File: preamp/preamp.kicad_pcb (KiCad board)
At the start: 2 copper layers, 19 parts, among them J1 XLR3_AudioJack2_Combo, J2 Output, J4 AudioJack3_Switch, U1 SSM2019

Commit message: Prepare for routing
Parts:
- C7: footprint Capacitor_THT:C_Disc_D3.0mm_W1.6mm_P2.50mm -> Capacitor_THT:C_Rect_L7.0mm_W2.5mm_P5.00mm
- J1: footprint Connector_Audio:Jack_XLR-6.35mm_Neutrik_NCJ9FI-V-0_Vertical -> Connector_Audio:Jack_XLR_Neutrik_NC3FAAH2_Horizontal
- moved R4 53.0 mm to (81.4, 43.4)
- moved BT1 52.8 mm to (148.8, 46.6)
- moved BT2 52.8 mm to (137.8, 46.6)
- moved C7 38.1 mm to (137.9, 79.2), turned to 90 degrees
- moved C4 37.9 mm to (97.1, 77.8), turned to 0 degrees
- moved R1 35.8 mm to (101.0, 73.6), turned to 0 degrees
- moved R3 35.6 mm to (101.1, 76.5), turned to 0 degrees
- moved C1 33.6 mm to (104.5, 68.4), turned to -90 degrees
- moved J1 33.4 mm to (111.2, 84.8), turned to -90 degrees
- moved C2 27.5 mm to (98.1, 81.9), turned to -90 degrees
- moved U1 19.1 mm to (128.4, 75.3), turned to 0 degrees
- moved C6 17.5 mm to (125.9, 79.8), turned to 90 degrees
- moved J2 17.3 mm to (147.0, 85.9), turned to 90 degrees
- moved C5 15.4 mm to (123.0, 63.1), turned to 0 degrees
- moved R5 15.2 mm to (135.9, 85.8), turned to 180 degrees
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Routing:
- net Net-(J2-Pad2): track 0.00 -> 23.7 mm
- net Net-(RV1-Pad3): track 0.00 -> 21.3 mm
- net Net-(C2-Pad1): track 0.00 -> 16.8 mm
- net Net-(R5-Pad2): track 0.00 -> 12.0 mm
- net Net-(R5-Pad1): track 0.00 -> 9.85 mm
- net Net-(C4-Pad2): track 0.00 -> 2.80 mm
- net Net-(C5-Pad2): track 0.00 -> 2.79 mm
- net Net-(U1-Pad6): track 0.00 -> 2.33 mm

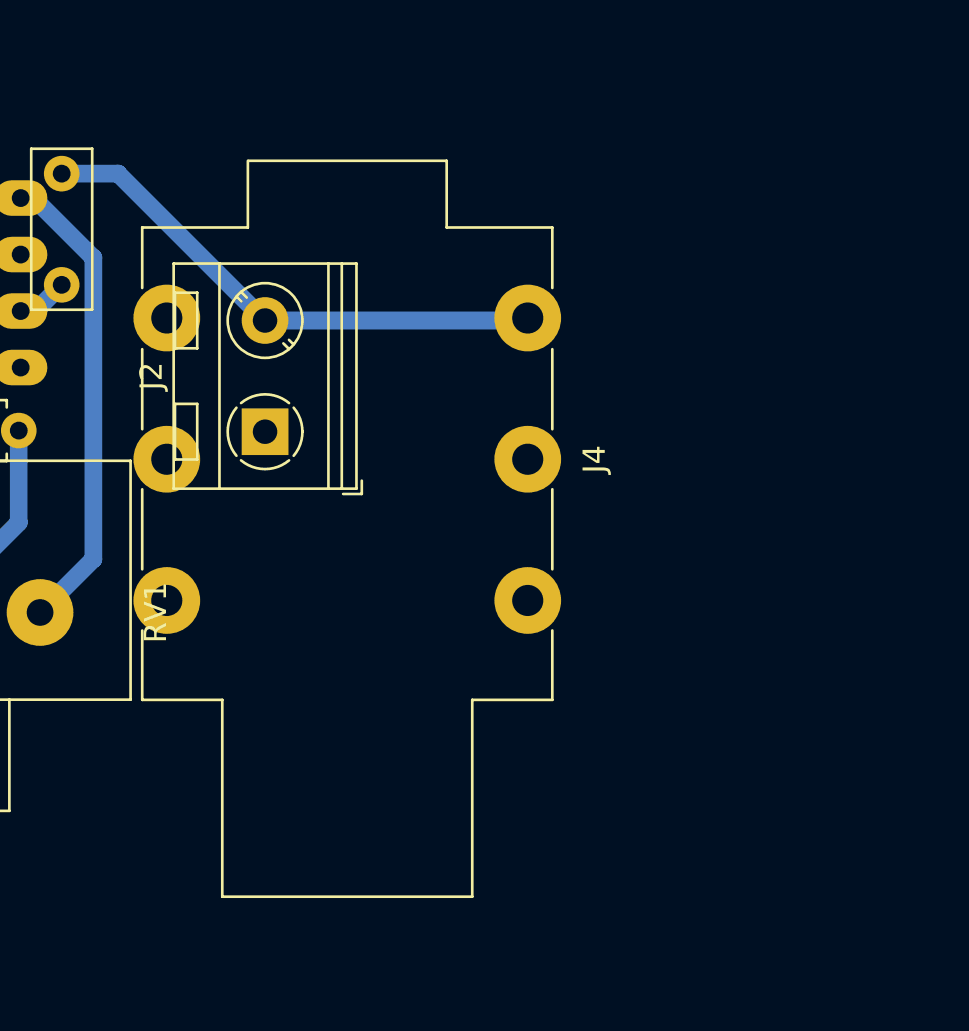
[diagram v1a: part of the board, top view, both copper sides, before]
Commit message: Add RCA Plug
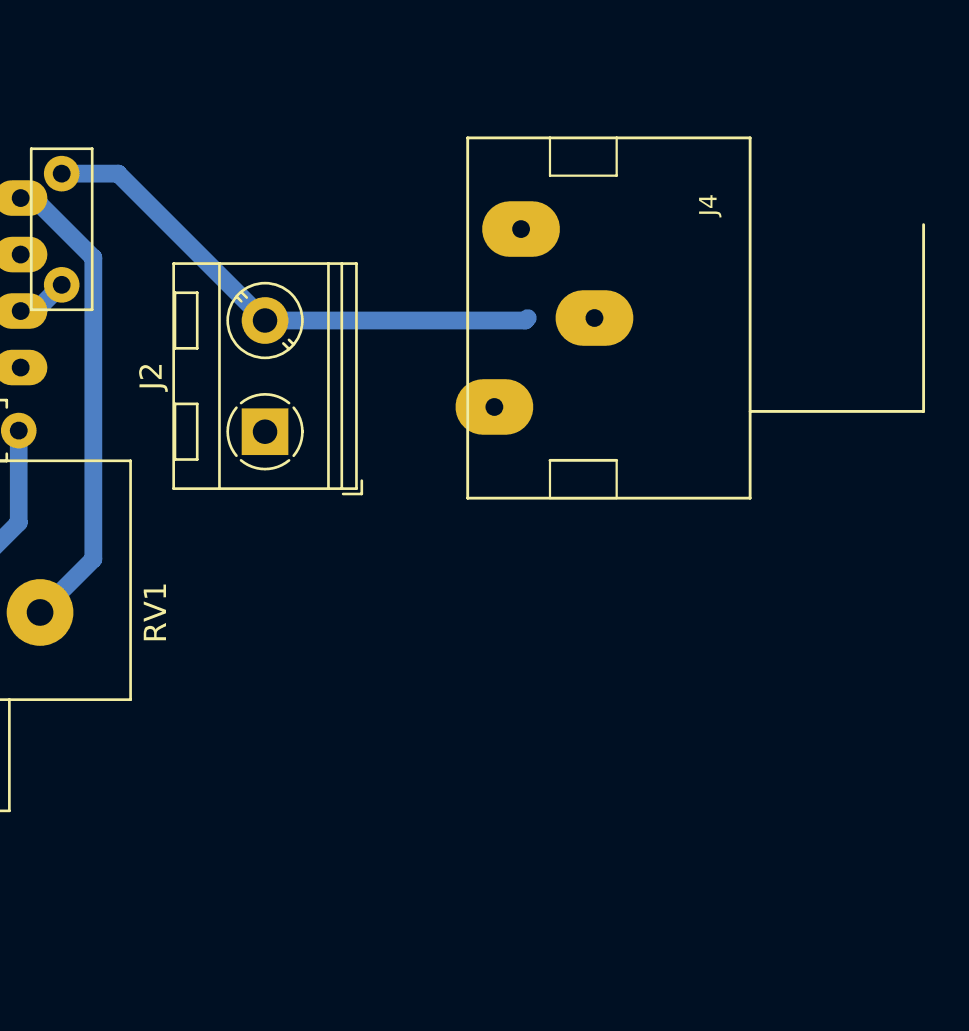
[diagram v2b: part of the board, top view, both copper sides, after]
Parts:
- J4: value AudioJack3_Switch -> RCJ-22; footprint Connector_Audio:Jack_6.35mm_Neutrik_NMJ6HFD2-AU_Horizontal -> rcj-22:rcj-22
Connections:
- C7 pad 2: Net-(J2-Pad2) -> Net-(C7-Pad2)
- J2 pad 2: Net-(J2-Pad2) -> Net-(C7-Pad2)
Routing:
- net Net-(J2-Pad2): track 23.7 -> 0.00 mm
- net Net-(C7-Pad2): track 0.00 -> 23.7 mm

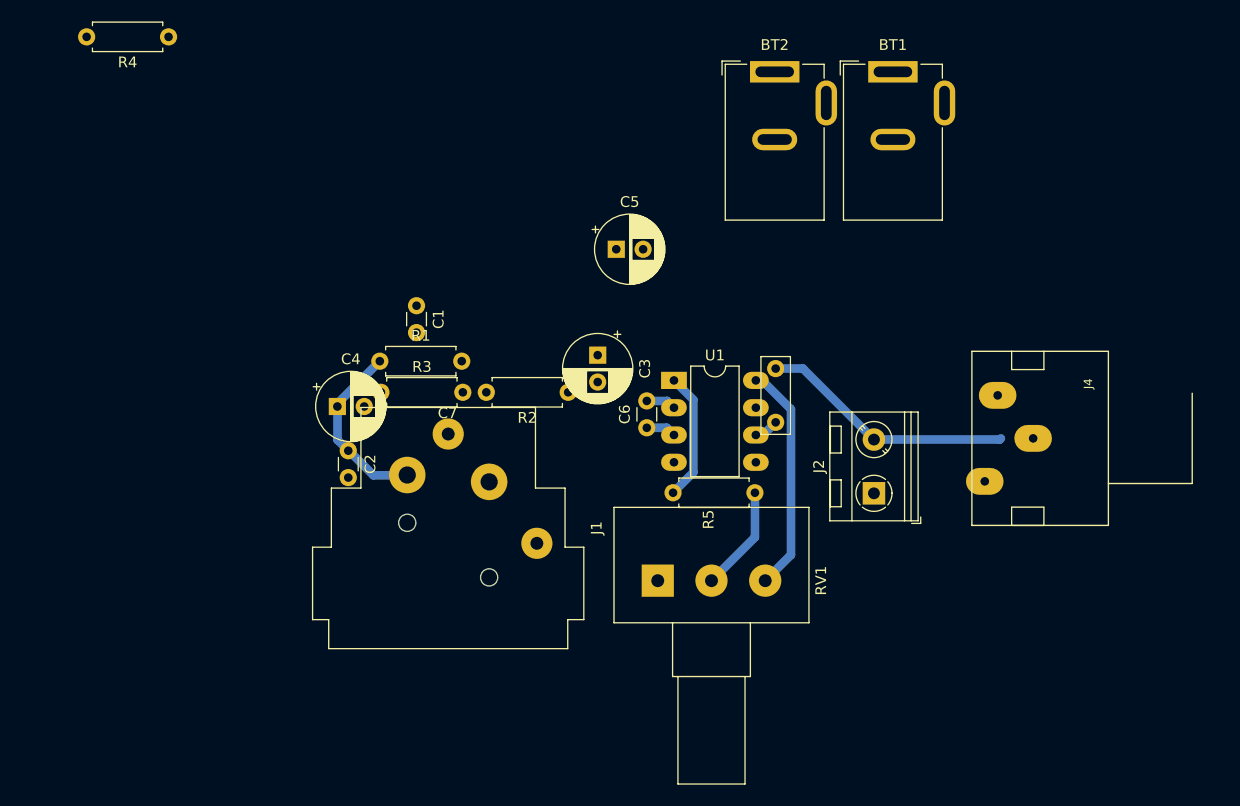
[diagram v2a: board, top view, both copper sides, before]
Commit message: Routing of preamp
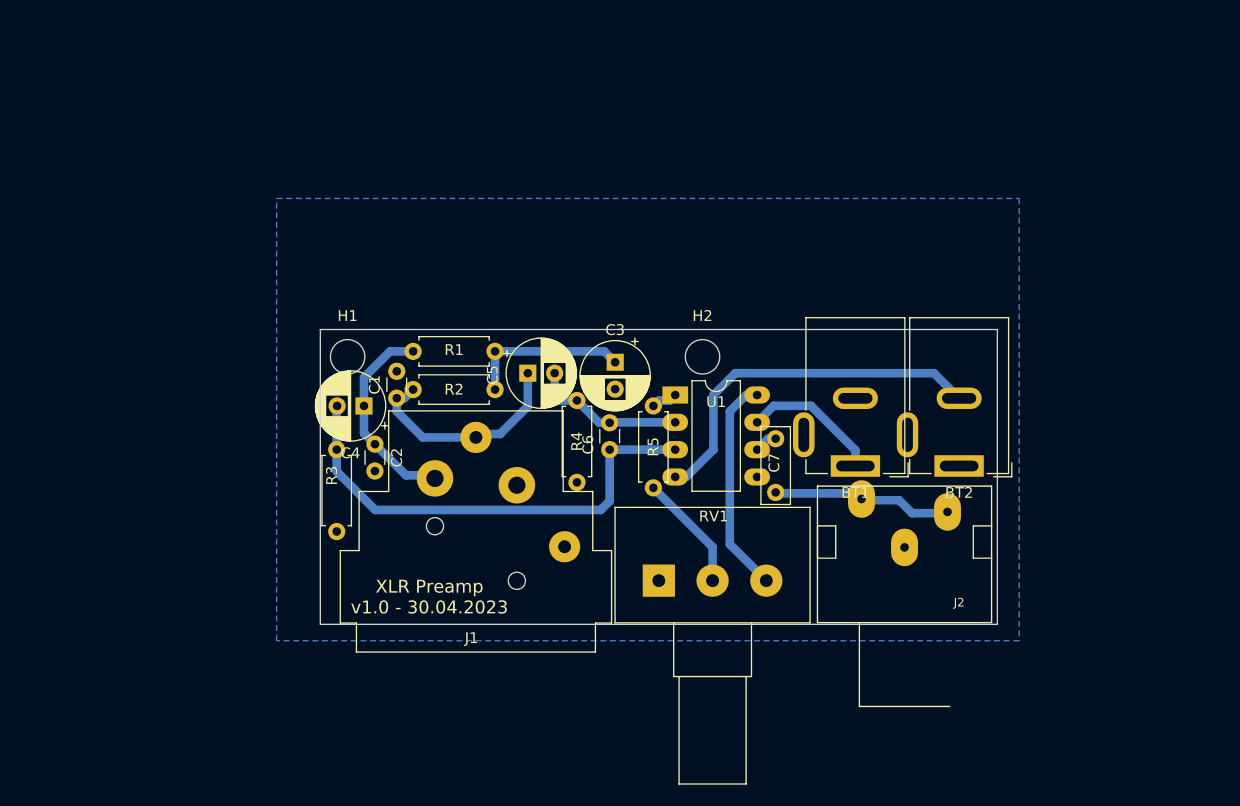
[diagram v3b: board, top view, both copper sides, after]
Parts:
- removed J4: RCJ-22, rcj-22:rcj-22
- added H1: MountingHole, MountingHole:MountingHole_3.2mm_M3_DIN965, F.Cu at (98.0, 73.2)
- added H2: MountingHole, MountingHole:MountingHole_3.2mm_M3_DIN965, F.Cu at (131.1, 73.2)
- J2: value Output -> RCJ-22; footprint TerminalBlock_RND:TerminalBlock_RND_205-00045_1x02_P5.00mm_Horizontal -> rcj-22:rcj-22
- moved R4 56.2 mm to (119.4, 84.8), turned to 90 degrees
- moved BT2 40.5 mm to (154.9, 83.3), turned to 180 degrees
- moved BT1 36.8 mm to (145.3, 83.3), turned to 180 degrees
- moved C5 14.2 mm to (114.8, 74.7)
- moved R5 9.46 mm to (126.5, 85.3), turned to 90 degrees
- moved C1 8.80 mm to (102.6, 77.0), turned to 90 degrees
- moved R2 6.81 mm to (111.8, 76.2)
- moved R3 6.74 mm to (97.0, 81.8), turned to -90 degrees
- moved C6 4.01 mm to (122.4, 81.8)
- moved J2 3.50 mm to (149.9, 87.9), turned to 180 degrees
- moved R1 3.23 mm to (104.1, 72.6)
- moved J1 2.60 mm to (113.8, 85.1)
- moved C2 2.55 mm to (100.6, 81.3)
- moved C4 2.48 mm to (99.6, 77.7), turned to 180 degrees
- moved C3 1.75 mm to (122.9, 73.7)
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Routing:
- net Net-(C4-Pad2): track 2.80 -> 44.2 mm
- net -15V: track 0.00 -> 34.4 mm
- net Net-(C1-Pad1): track 0.00 -> 20.6 mm
- net Net-(C3-Pad1): track 0.00 -> 15.2 mm
- net +15V: track 0.00 -> 13.0 mm
- net Net-(C5-Pad2): track 2.79 -> 14.3 mm
- net Net-(R5-Pad2): track 12.0 -> 2.45 mm
- net Net-(C7-Pad2): track 23.7 -> 16.8 mm
- net Net-(C2-Pad1): track 16.8 -> 19.1 mm
- net Net-(R5-Pad1): track 9.85 -> 10.9 mm
- net Net-(RV1-Pad3): track 21.3 -> 20.3 mm
- added copper zone on B.Cu, net GNDA
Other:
- board outline added: 63 x 27.4 mm
- board text added: "XLR Preamp v1.0 - 30.04.2023"

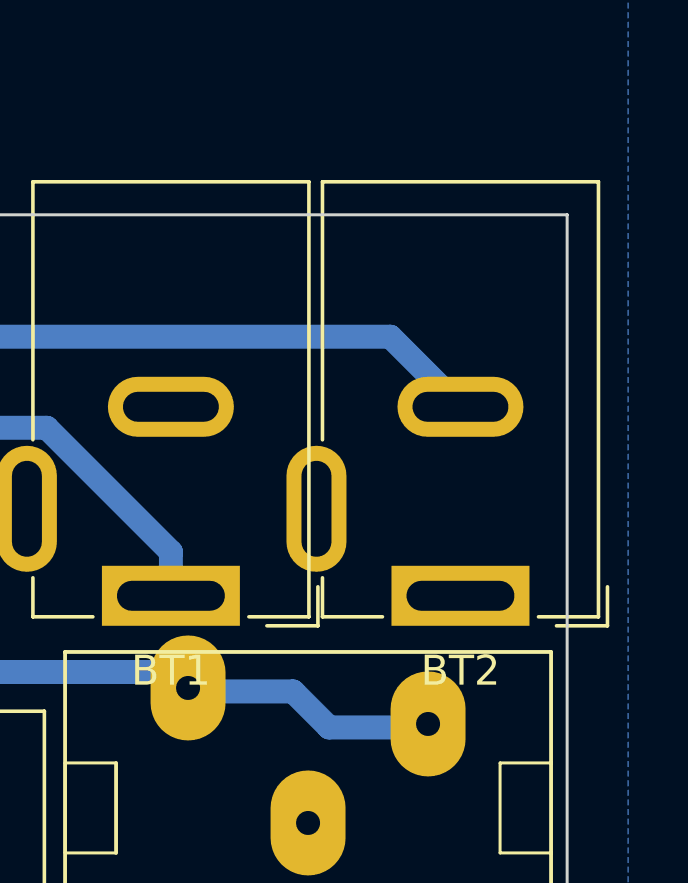
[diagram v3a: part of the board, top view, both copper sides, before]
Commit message: Add 3d models
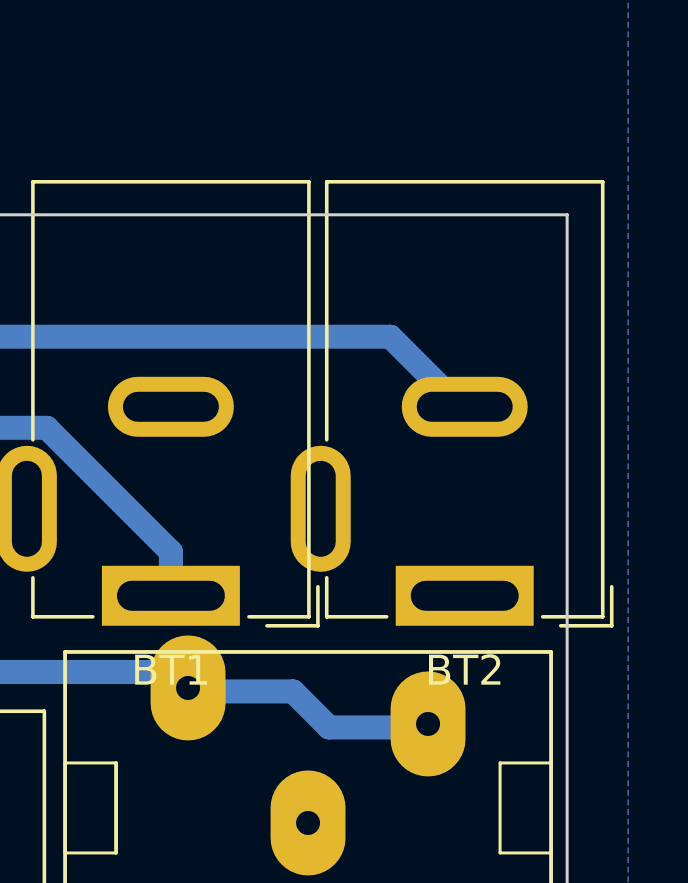
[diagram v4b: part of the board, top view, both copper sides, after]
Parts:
- moved BT2 0.14 mm to (155.1, 83.3)
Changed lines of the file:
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@@
       (rotate (xyz 0 0 0))
+    )
+    (model "${KIPRJMOD}/lib/potentiometer.step"
+      (offset (xyz 5.75 -5 12.5))
+      (scale (xyz 1 1 1))
+      (rotate (xyz 90 -180 -90))
     )
   )
@@
       (scale (xyz 1 1 1))
       (rotate (xyz 0 0 0))
+    )
+  )
+  (footprint "Connector_BarrelJack:BarrelJack_GCT_DCJ200-10-A_Horizontal" (layer "F.Cu")
+    (at 155.082 83.312 180)
+    (descr "Barrel jack connector (5.5 mm outer diameter, 2.05 inner diameter ), https://gct.co/files/drawings/dcj200-10.pdf")
+    (tags "connector barrel jack")
+    (property "Sheetfile" "preamp.kicad_sch")
+    (property "Sheetname" "")
+    (attr through_hole)
+    (fp_text reference "BT2" (at 0 -2.5) (layer "F.SilkS")
+      (effects (font (size 1 1) (thickness 0.15)))
+    )
+    (fp_text value "Battery_Cell" (at 0 15.5) (layer "F.Fab")
+      (effects (font (size 1 1) (thickness 0.15)))
+    )
+    (fp_text user "${REFERENCE}" (at 0 3) (layer "F.Fab")
+      (effects (font (size 1 1) (thickness 0.15)))
+    )
+    (fp_line (start -4.6 13.8) (end -4.6 -0.7) (layer "F.SilkS") (width 0.12))
+    (fp_line (start -4.6 -0.7) (end -2.6 -0.7) (layer "F.SilkS") (width 0.12))
+    (fp_line (start 4.6 13.8) (end -4.6 13.8) (layer "F.SilkS") (width 0.12))
+    (fp_line (start 2.6 -0.7) (end 4.6 -0.7) (layer "F.SilkS") (width 0.12))
+    (fp_line (start 4.6 5.2) (end 4.6 13.8) (layer "F.SilkS") (width 0.12))
+    (fp_line (start 4.6 -0.7) (end 4.6 0.6) (layer "F.SilkS") (width 0.12))
+    (fp_line (start -4.9 -1) (end -4.9 0.3) (layer "F.SilkS") (width 0.12))
+    (fp_line (start -3.2 -1) (end -4.9 -1) (layer "F.SilkS") (width 0.12))
+    (fp_line (start 6.3 5.5) (end 5 5.5) (layer "F.CrtYd") (width 0.05))
+    (fp_line (start 5 -1.5) (end -5 -1.5) (layer "F.CrtYd") (width 0.05))
+    (fp_line (start 5 14.2) (end 5 5.5) (layer "F.CrtYd") (width 0.05))
+    (fp_line (start -5 14.2) (end 5 14.2) (layer "F.CrtYd") (width 0.05))
+    (fp_line (start 6.3 0.3) (end 6.3 5.5) (layer "F.CrtYd") (width 0.05))
+    (fp_line (start -5 -1.5) (end -5 14.2) (layer "F.CrtYd") (width 0.05))
+    (fp_line (start 5 0.3) (end 5 -1.5) (layer "F.CrtYd") (width 0.05))
+    (fp_line (start 6.3 0.3) (end 5 0.3) (layer "F.CrtYd") (width 0.05))
+    (fp_line (start 4.5 13.7) (end -4.5 13.7) (layer "F.Fab") (width 0.1))
+    (fp_line (start 4.5 -0.6) (end 4.5 13.7) (layer "F.Fab") (width 0.1))
+    (fp_line (start -4.5 13.7) (end -4.5 0.4) (layer "F.Fab") (width 0.1))
+    (fp_line (start -4.5 0.4) (end -3.5 -0.6) (layer "F.Fab") (width 0.1))
+    (fp_line (start 4.5 -0.6) (end -3.5 -0.6) (layer "F.Fab") (width 0.1))
+    (pad "1" thru_hole rect (at 0 0 180) (size 4.6 2) (drill oval 3.6 1) (layers *.Cu *.Mask)
+      (net 2 "GNDA") (pinfunction "+") (pintype "passive"))
+    (pad "2" thru_hole oval (at 0 6.3 180) (size 4.2 2) (drill oval 3.2 1) (layers *.Cu *.Mask)
+      (net 8 "-15V") (pinfunction "-") (pintype "passive"))
+    (pad "3" thru_hole oval (at 4.8 2.9 180) (size 2 4.2) (drill oval 1 3.2) (layers *.Cu *.Mask))
+    (model "${KICAD6_3DMODEL_DIR}/Connector_BarrelJack.3dshapes/BarrelJack_GCT_DCJ200-10-A_Horizontal.wrl"
+      (offset (xyz 0 0 0))
+      (scale (xyz 1 1 1))
+      (rotate (xyz 0 0 0))
+    )
+    (model "${KIPRJMOD}/lib/DS-210.step"
+      (offset (xyz 0 -13.75 0))
+      (scale (xyz 1 1 1))
+      (rotate (xyz 0 0 -180))
     )
   )
@@
       (rotate (xyz 0 0 0))
     )
+    (model "${KIPRJMOD}/lib/NC3FAAH2.step"
+      (offset (xyz -10.25 -3.75 -1.7))
+      (scale (xyz 1 1 1))
+      (rotate (xyz 0 0 90))
+    )
   )
   (footprint "Capacitor_THT:C_Disc_D3.0mm_W1.6mm_P2.50mm" (layer "F.Cu")
@@
     )
   )
-  (footprint "Connector_BarrelJack:BarrelJack_GCT_DCJ200-10-A_Horizontal" (layer "F.Cu")
-    (at 154.94 83.312 180)
-    (descr "Barrel jack connector (5.5 mm outer diameter, 2.05 inner diameter ), https://gct.co/files/drawings/dcj200-10.pdf")
-    (tags "connector barrel jack")
-    (property "Sheetfile" "preamp.kicad_sch")
-    (property "Sheetname" "")
-    (attr through_hole)
-    (fp_text reference "BT2" (at 0 -2.5) (layer "F.SilkS")
-      (effects (font (size 1 1) (thickness 0.15)))
-    )
-    (fp_text value "Battery_Cell" (at 0 15.5) (layer "F.Fab")
-      (effects (font (size 1 1) (thickness 0.15)))
-    )
-    (fp_text user "${REFERENCE}" (at 0 3) (layer "F.Fab")
-      (effects (font (size 1 1) (thickness 0.15)))
-    )
-    (fp_line (start 4.6 13.8) (end -4.6 13.8) (layer "F.SilkS") (width 0.12))
-    (fp_line (start 4.6 -0.7) (end 4.6 0.6) (layer "F.SilkS") (width 0.12))
-    (fp_line (start -3.2 -1) (end -4.9 -1) (layer "F.SilkS") (width 0.12))
-    (fp_line (start 4.6 5.2) (end 4.6 13.8) (layer "F.SilkS") (width 0.12))
-    (fp_line (start 2.6 -0.7) (end 4.6 -0.7) (layer "F.SilkS") (width 0.12))
-    (fp_line (start -4.9 -1) (end -4.9 0.3) (layer "F.SilkS") (width 0.12))
-    (fp_line (start -4.6 13.8) (end -4.6 -0.7) (layer "F.SilkS") (width 0.12))
-    (fp_line (start -4.6 -0.7) (end -2.6 -0.7) (layer "F.SilkS") (width 0.12))
-    (fp_line (start -5 -1.5) (end -5 14.2) (layer "F.CrtYd") (width 0.05))
-    (fp_line (start 5 -1.5) (end -5 -1.5) (layer "F.CrtYd") (width 0.05))
-    (fp_line (start 6.3 0.3) (end 5 0.3) (layer "F.CrtYd") (width 0.05))
-    (fp_line (start 5 0.3) (end 5 -1.5) (layer "F.CrtYd") (width 0.05))
-    (fp_line (start 6.3 5.5) (end 5 5.5) (layer "F.CrtYd") (width 0.05))
-    (fp_line (start 5 14.2) (end 5 5.5) (layer "F.CrtYd") (width 0.05))
-    (fp_line (start 6.3 0.3) (end 6.3 5.5) (layer "F.CrtYd") (width 0.05))
-    (fp_line (start -5 14.2) (end 5 14.2) (layer "F.CrtYd") (width 0.05))
-    (fp_line (start 4.5 -0.6) (end 4.5 13.7) (layer "F.Fab") (width 0.1))
-    (fp_line (start -4.5 13.7) (end -4.5 0.4) (layer "F.Fab") (width 0.1))
-    (fp_line (start 4.5 -0.6) (end -3.5 -0.6) (layer "F.Fab") (width 0.1))
-    (fp_line (start -4.5 0.4) (end -3.5 -0.6) (layer "F.Fab") (width 0.1))
-    (fp_line (start 4.5 13.7) (end -4.5 13.7) (layer "F.Fab") (width 0.1))
-    (pad "1" thru_hole rect (at 0 0 180) (size 4.6 2) (drill oval 3.6 1) (layers *.Cu *.Mask)
-      (net 2 "GNDA") (pinfunction "+") (pintype "passive"))
-    (pad "2" thru_hole oval (at 0 6.3 180) (size 4.2 2) (drill oval 3.2 1) (layers *.Cu *.Mask)
-      (net 8 "-15V") (pinfunction "-") (pintype "passive"))
-    (pad "3" thru_hole oval (at 4.8 2.9 180) (size 2 4.2) (drill oval 1 3.2) (layers *.Cu *.Mask))
-    (model "${KICAD6_3DMODEL_DIR}/Connector_BarrelJack.3dshapes/BarrelJack_GCT_DCJ200-10-A_Horizontal.wrl"
-      (offset (xyz 0 0 0))
-      (scale (xyz 1 1 1))
-      (rotate (xyz 0 0 0))
-    )
-  )
   (footprint "Capacitor_THT:C_Disc_D3.0mm_W1.6mm_P2.50mm" (layer "F.Cu")
     (at 100.584 81.28 -90)
@@
       (rotate (xyz 0 0 0))
     )
-  )
+    (model "${KIPRJMOD}/lib/DS-210.step"
+      (offset (xyz 0 -13.75 0))
+      (scale (xyz 1 1 1))
+      (rotate (xyz 0 0 -180))
+    )
+  )
